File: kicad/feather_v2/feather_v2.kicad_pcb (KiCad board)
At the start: 2 copper layers, 50.8 x 22.9 mm, 8 parts, among them P1 Maniacal Labs, P10 WyoLum, P2 Screw, P3 Screw, P6 Input, P7 Output, P8 Feather_M0

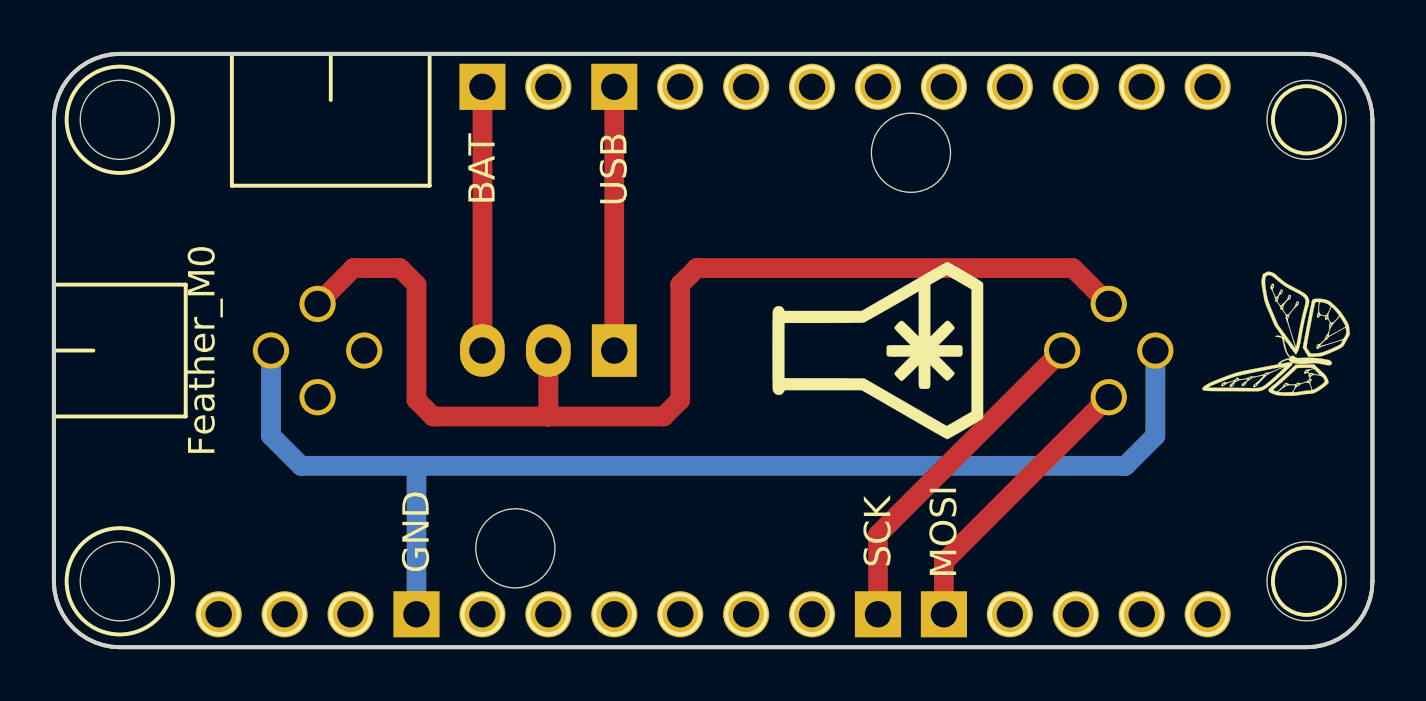
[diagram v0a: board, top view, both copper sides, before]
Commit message: feather_v2 added SMD shorting links and extra power switch
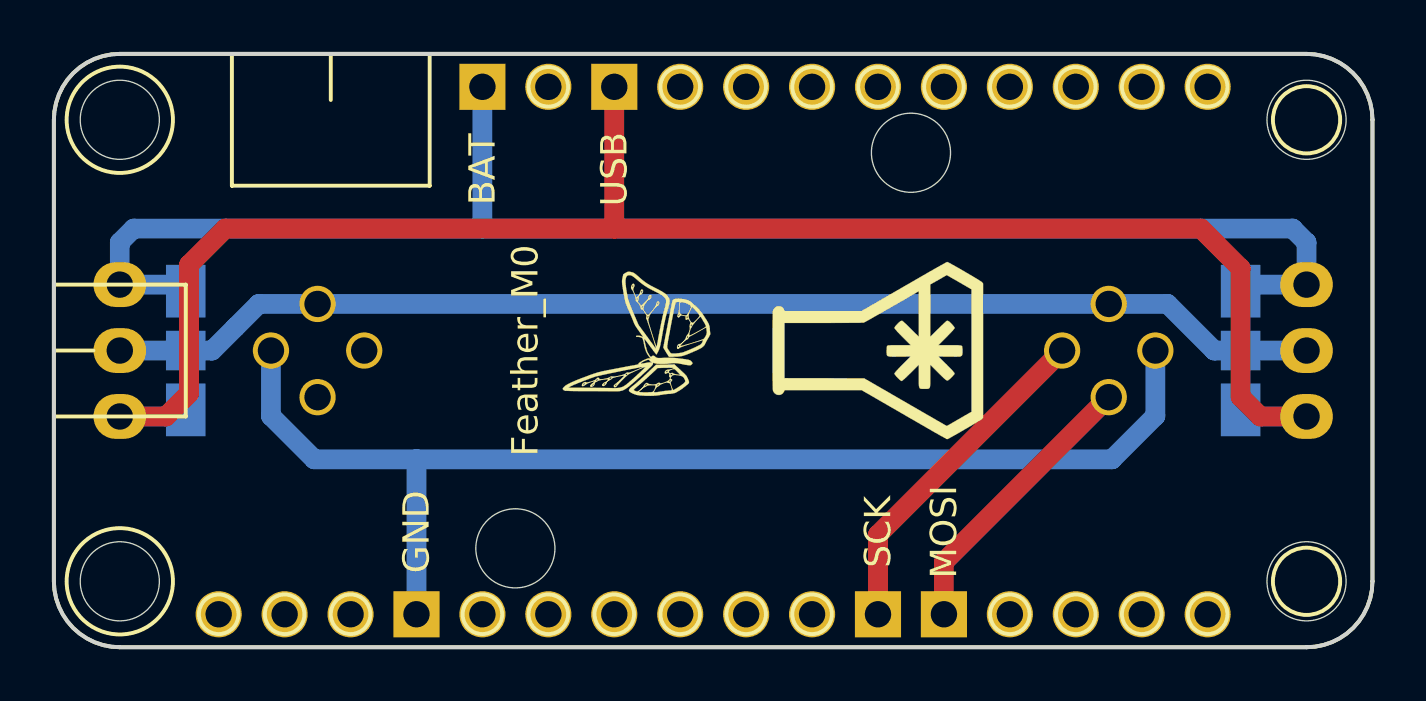
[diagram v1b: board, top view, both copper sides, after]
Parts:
- added JP2: PWR_SEL2, feather_v2:switch_spdt, B.Cu at (78.7, 101.6)
- JP1: footprint feather_v2:Pin_Header_Straight_1x03 -> feather_v2:switch_spdt
- moved JP1 26.7 mm to (124.5, 101.6), turned to 180 degrees
- moved P10 24.6 mm to (99.2, 101.6)
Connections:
- JP1 pad 1: /VUSB -> /VBAT
- JP1 pad 3: /VBAT -> /VUSB
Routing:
- net /VUSB: track 10.2 -> 68.1 mm
- net /VBAT: track 10.2 -> 60.0 mm
- net /VLED: track 44.1 -> 47.2 mm
- net /GND: track 47.3 -> 46.5 mm
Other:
- board text added: "BAT< >USB"
- board text removed: "BAT<>USB"
